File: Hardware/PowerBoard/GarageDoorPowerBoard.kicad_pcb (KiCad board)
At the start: 2 copper layers, 12 parts, among them J1 1984617, J2 JST-PH2, J3 JST-PH2, J4 JST-PH2, J5 RJ45

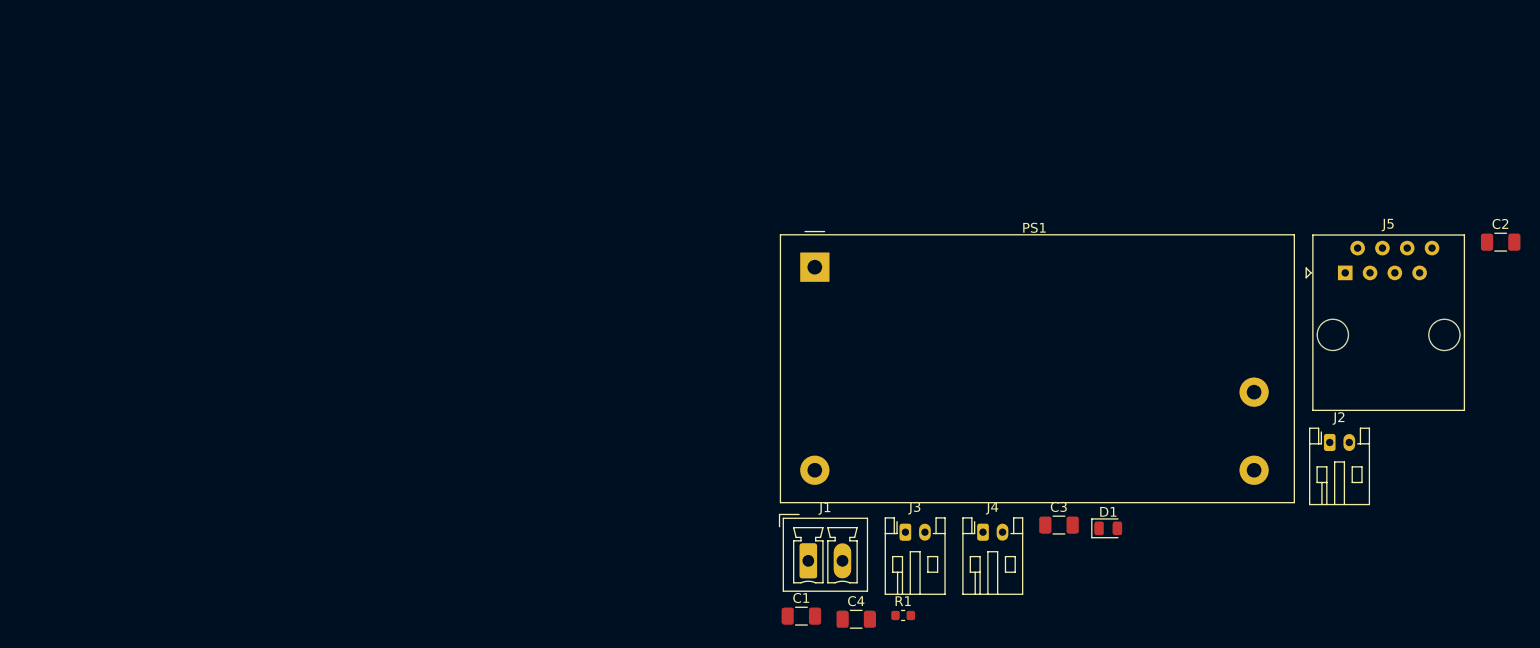
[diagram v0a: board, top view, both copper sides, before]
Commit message: started work on the power PCB, board shape and basic placement complete
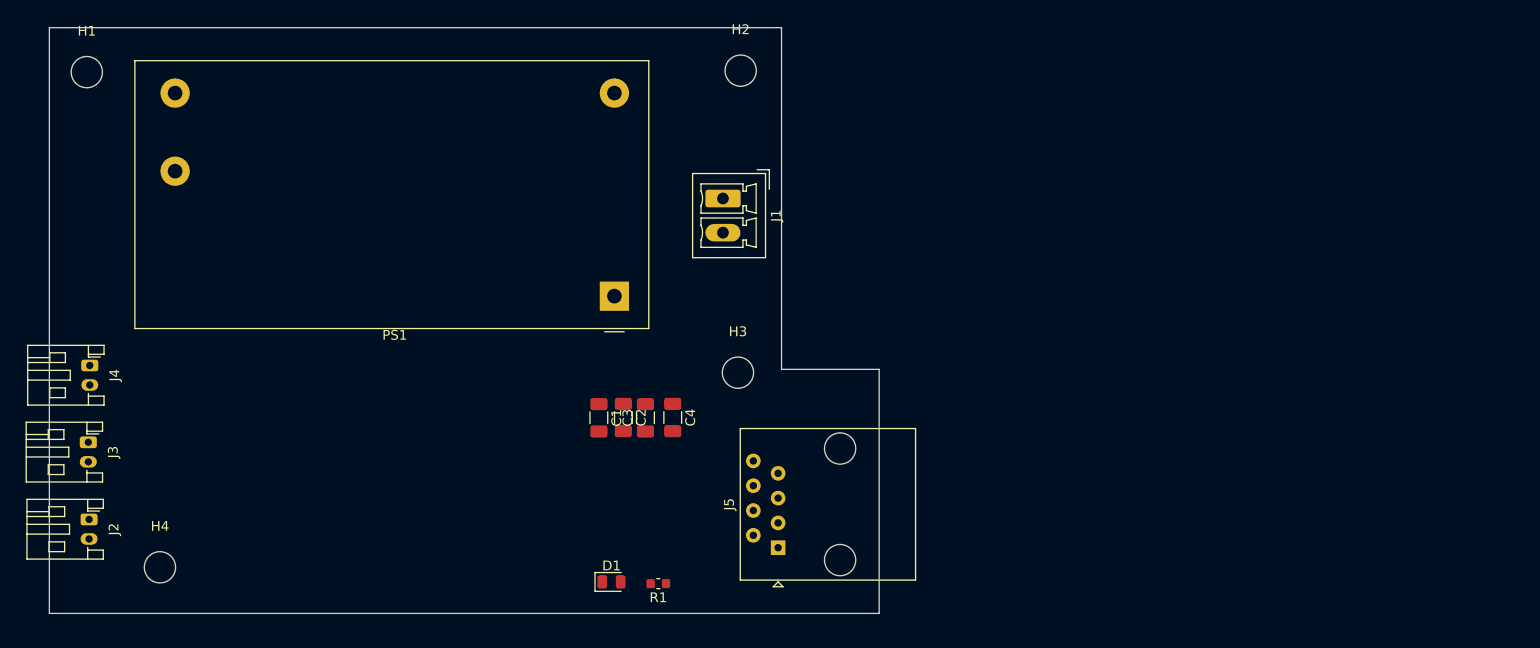
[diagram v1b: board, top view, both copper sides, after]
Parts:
- added H1: MountingHole, MountingHole:MountingHole_3.2mm_M3, F.Cu at (105.4, 66.5)
- added H2: MountingHole, MountingHole:MountingHole_3.2mm_M3, F.Cu at (172.4, 66.3)
- added H3: MountingHole, MountingHole:MountingHole_3.2mm_M3, F.Cu at (172.1, 97.3)
- added H4: MountingHole, MountingHole:MountingHole_3.2mm_M3, F.Cu at (112.9, 117.2)
- moved J2 127.3 mm to (105.7, 112.3), turned to 270 degrees
- moved J4 93.1 mm to (105.7, 96.5), turned to 270 degrees
- moved C2 91.6 mm to (160.4, 101.9), turned to 270 degrees
- moved J3 84.2 mm to (105.6, 104.4), turned to 270 degrees
- moved J5 64.6 mm to (176.3, 115.2), turned to 90 degrees
- moved D1 51.2 mm to (159.2, 118.7)
- moved C3 43.8 mm to (162.7, 101.9), turned to 90 degrees
- moved J1 38.1 mm to (170.6, 79.4), turned to 270 degrees
- moved C1 29.0 mm to (157.9, 101.9), turned to 270 degrees
- moved C4 27.9 mm to (165.5, 101.9), turned to 270 degrees
- moved R1 25.3 mm to (164.0, 118.9), turned to 180 degrees
- moved PS1 20.7 mm to (159.5, 89.4), turned to 180 degrees
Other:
- board outline added: 85 x 60 mm

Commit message: PCB finished for power board
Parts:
- moved H4 6.33 mm to (106.6, 116.9)
- moved J4 5.65 mm to (105.0, 90.9)
- moved J3 5.51 mm to (105.0, 98.9)
- moved J2 5.42 mm to (105.0, 106.9)
- moved R1 4.00 mm to (165.0, 115.0)
- moved D1 3.78 mm to (160.0, 115.0)
- moved J5 1.46 mm to (175.5, 113.9)
- moved H1 1.25 mm to (106.6, 66.9)
- moved C3 1.22 mm to (163.5, 101.0), turned to 270 degrees
- moved C1 1.07 mm to (158.5, 101.0)
- moved C2 1.04 mm to (161.0, 101.0)
- moved PS1 1.02 mm to (160.5, 89.4)
- moved C4 1.01 mm to (166.0, 101.0)
- moved H2 1.01 mm to (171.6, 66.9)
- moved H3 0.54 mm to (171.6, 97.3)
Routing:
- net +24V: track 0.00 -> 95.2 mm
- net /REED_SW1_IN: track 0.00 -> 76.1 mm
- net /REED_SW1_GND: track 0.00 -> 73.9 mm
- net /REED_SW2_IN: track 0.00 -> 73.8 mm
- net /REED_SW2_GND: track 0.00 -> 71.6 mm
- net /Relay_Output1: track 0.00 -> 71.6 mm
- net /Relay_Output2: track 0.00 -> 69.3 mm
- net Net-(J1-Pad1): track 0.00 -> 16.9 mm
- net Net-(J1-Pad2): track 0.00 -> 14.0 mm
- net Net-(D1-Pad2): track 0.00 -> 3.28 mm
- net GND: vias 0 -> 37
- added copper zone on B.Cu, net GND
- added copper zone on F.Cu, net GND
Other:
- outline, holes or cut-outs redrawn
- board text added: "120 AC -> 24V Converter"
- board text added: "AC/L"
- board text added: "AC/N"
- board text added: "Martian Engineering Matthew Glazer Garage Door Power Board Rev1a"
- board text added: "Power/Control RJ45 connect"
- board text added: "RELAY 2 REED 2 REED 1"
- board text added: "WARN: 120V AC"

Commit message: minor tweaks as I was making a readme
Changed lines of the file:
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@@
   )
   (setup
-    (last_trace_width 0.5)
+    (last_trace_width 0.25)
     (user_trace_width 0.35)
     (user_trace_width 0.5)
@@
     (tags "mounting hole 3.2mm no annular m3")
     (attr virtual)
-    (fp_text reference H4 (at 0 -4.2) (layer F.SilkS)
+    (fp_text reference H4 (at -0.0216 -2.874) (layer F.SilkS)
       (effects (font (size 1 1) (thickness 0.15)))
     )
@@
     (tags "mounting hole 3.2mm no annular m3")
     (attr virtual)
-    (fp_text reference H3 (at 0 -4.2) (layer F.SilkS)
+    (fp_text reference H3 (at -0.0738 -2.8448) (layer F.SilkS)
       (effects (font (size 1 1) (thickness 0.15)))
     )
@@
     (tags "mounting hole 3.2mm no annular m3")
     (attr virtual)
-    (fp_text reference H2 (at 0 -4.2) (layer F.SilkS)
+    (fp_text reference H2 (at -0.023 -2.6072) (layer F.SilkS)
       (effects (font (size 1 1) (thickness 0.15)))
     )
@@
     (tags "mounting hole 3.2mm no annular m3")
     (attr virtual)
-    (fp_text reference H1 (at 0 -4.2) (layer F.SilkS)
+    (fp_text reference H1 (at -0.0216 -2.8358) (layer F.SilkS)
       (effects (font (size 1 1) (thickness 0.15)))
     )
